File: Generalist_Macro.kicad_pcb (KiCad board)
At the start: 2 copper layers, 50.4 x 60.7 mm, 7 parts, among them SW1 SW_Push, SW2 SW_Push, SW3 SW_Push, SW4 SW_Push, U1 XIAO-RP2040-DIP

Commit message: Finished Schematic, Started PCB
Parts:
- removed SW4: SW_Push, Button_Switch_Keyboard:SW_Cherry_MX_1.00u_PCB
- added D10: WS2812B, LED_SMD:LED_WS2812B_PLCC4_5.0x5.0mm_P3.2mm, F.Cu at (160.0, 96.7)
- added D11: WS2812B, LED_SMD:LED_WS2812B_PLCC4_5.0x5.0mm_P3.2mm, F.Cu at (185.8, 63.2)
- added D12: WS2812B, LED_SMD:LED_WS2812B_PLCC4_5.0x5.0mm_P3.2mm, F.Cu at (185.8, 69.8)
- added D13: WS2812B, LED_SMD:LED_WS2812B_PLCC4_5.0x5.0mm_P3.2mm, F.Cu at (101.0, 56.0)
- added D14: WS2812B, LED_SMD:LED_WS2812B_PLCC4_5.0x5.0mm_P3.2mm, F.Cu at (160.2, 83.2)
- added D15: WS2812B, LED_SMD:LED_WS2812B_PLCC4_5.0x5.0mm_P3.2mm, F.Cu at (193.9, 63.2)
- added D16: WS2812B, LED_SMD:LED_WS2812B_PLCC4_5.0x5.0mm_P3.2mm, F.Cu at (193.9, 69.8)
- added D17: WS2812B, LED_SMD:LED_WS2812B_PLCC4_5.0x5.0mm_P3.2mm, F.Cu at (116.2, 56.0)
- added D18: WS2812B, LED_SMD:LED_WS2812B_PLCC4_5.0x5.0mm_P3.2mm, F.Cu at (160.2, 69.7)
- added D19: WS2812B, LED_SMD:LED_WS2812B_PLCC4_5.0x5.0mm_P3.2mm, F.Cu at (202.1, 63.2)
- added D20: WS2812B, LED_SMD:LED_WS2812B_PLCC4_5.0x5.0mm_P3.2mm, F.Cu at (202.1, 69.8)
- added D21: WS2812B, LED_SMD:LED_WS2812B_PLCC4_5.0x5.0mm_P3.2mm, F.Cu at (131.5, 56.0)
- added D22: WS2812B, LED_SMD:LED_WS2812B_PLCC4_5.0x5.0mm_P3.2mm, F.Cu at (160.6, 56.2)
- added D23: WS2812B, LED_SMD:LED_WS2812B_PLCC4_5.0x5.0mm_P3.2mm, F.Cu at (210.2, 63.2)
- added D24: WS2812B, LED_SMD:LED_WS2812B_PLCC4_5.0x5.0mm_P3.2mm, F.Cu at (210.2, 69.8)
- added D3: 1N4148WT, Diode_SMD:D_SOD-523, F.Cu at (64.5, 89.8)
- added D4: 1N4148WT, Diode_SMD:D_SOD-523, F.Cu at (74.0, 89.8)
- added D5: 1N4148WT, Diode_SMD:D_SOD-523, F.Cu at (64.5, 82.9)
- added D6: 1N4148WT, Diode_SMD:D_SOD-523, F.Cu at (74.0, 82.9)
- added D7: 1N4148WT, Diode_SMD:D_SOD-523, F.Cu at (74.0, 76.0)
- added D8: 1N4148WT, Diode_SMD:D_SOD-523, F.Cu at (64.5, 76.0)
- added D9: WS2812B, LED_SMD:LED_WS2812B_PLCC4_5.0x5.0mm_P3.2mm, F.Cu at (85.7, 56.0)
- added J1: OLED_DISPLAY, Connector_PinHeader_2.54mm:PinHeader_1x04_P2.54mm_Vertical, F.Cu at (141.4, 56.6)
- added SW13: RotaryEncoder_Switch, Rotary_Encoder:RotaryEncoder_Alps_EC11E-Switch_Vertical_H20mm, F.Cu at (137.8, 68.1)
- added SW5: SW_Push, Button_Switch_Keyboard:SW_Cherry_MX_1.00u_PCB, F.Cu at (141.8, 94.8)
- added SW6: SW_Push, Button_Switch_Keyboard:SW_Cherry_MX_1.00u_PCB, F.Cu at (88.9, 75.9)
- added SW7: SW_Push, Button_Switch_Keyboard:SW_Cherry_MX_1.00u_PCB, F.Cu at (104.0, 75.9)
- added SW8: SW_Push, Button_Switch_Keyboard:SW_Cherry_MX_1.00u_PCB, F.Cu at (122.9, 75.9)
- D1, D2: value SK6812MINI -> 1N4148WT; footprint LED_SMD:LED_SK6812MINI_PLCC4_3.5x3.5mm_P1.75mm -> Diode_SMD:D_SOD-523
- moved D2 155.5 mm to (64.5, 96.7), turned to 180 degrees
- moved U1 135.0 mm to (69.2, 61.7)
- moved D1 113.1 mm to (74.0, 96.7), turned to 180 degrees
- moved SW2 110.8 mm to (103.8, 95.0), turned to 180 degrees
- moved SW1 106.8 mm to (88.7, 95.0), turned to 180 degrees
- moved SW3 76.5 mm to (122.8, 94.9), turned to 180 degrees
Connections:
- D1 pad 1: Net-(D1-DOUT) -> Net-(D1-K)
- D1 pad 2: GND -> Net-(D1-A)
- D2 pad 1: unconnected-(D2-DOUT-Pad1) -> Net-(D1-K)
- D2 pad 2: GND -> Net-(D2-A)
- SW1 pad 1: GND -> Net-(D1-A)
- SW1 pad 2: Net-(U1-GPIO1/RX) -> Net-(U1-GPIO26/ADC0/A0)
- SW2 pad 1: GND -> Net-(D2-A)
- SW2 pad 2: Net-(U1-GPIO2/SCK) -> Net-(U1-GPIO27/ADC1/A1)
- SW3 pad 1: GND -> Net-(D3-A)
- SW3 pad 2: Net-(U1-GPIO4/MISO) -> Net-(U1-GPIO28/ADC2/A2)
- U1 pad 1: unconnected-(U1-GPIO26/ADC0/A0-Pad1) -> Net-(U1-GPIO26/ADC0/A0)
- U1 pad 10: Net-(U1-GPIO4/MISO) -> Net-(U1-GPIO3/MOSI)
- U1 pad 2: unconnected-(U1-GPIO27/ADC1/A1-Pad2) -> Net-(U1-GPIO27/ADC1/A1)
- U1 pad 3: unconnected-(U1-GPIO28/ADC2/A2-Pad3) -> Net-(U1-GPIO28/ADC2/A2)
- U1 pad 4: unconnected-(U1-GPIO29/ADC3/A3-Pad4) -> Net-(U1-GPIO29/ADC3/A3)
- U1 pad 5: Net-(D1-DIN) -> Net-(J1-Pin_1)
- U1 pad 6: unconnected-(U1-GPIO7/SCL-Pad6) -> Net-(J1-Pin_2)
- U1 pad 7: unconnected-(U1-GPIO0/TX-Pad7) -> Net-(D1-K)
- U1 pad 8: Net-(U1-GPIO1/RX) -> Net-(D18-DIN)
- U1 pad 9: Net-(U1-GPIO2/SCK) -> Net-(D5-K)
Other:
- board outline removed

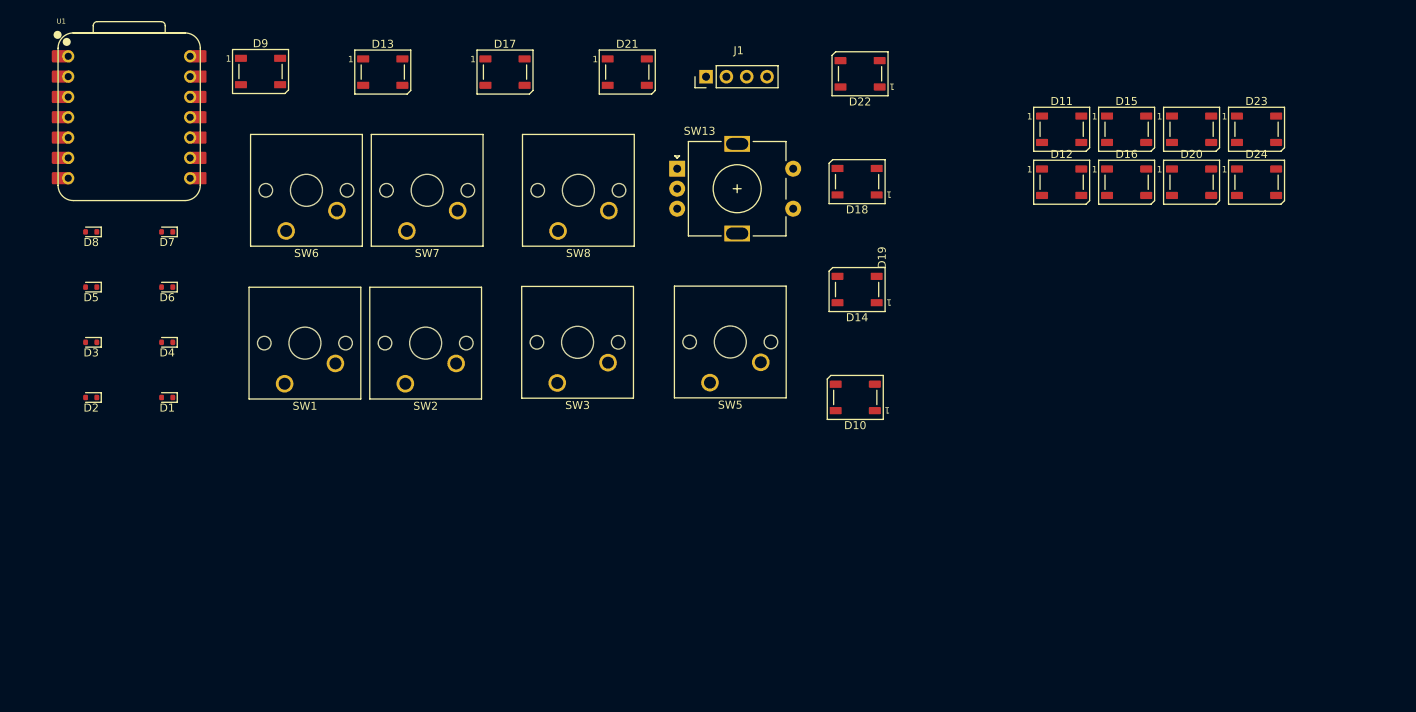
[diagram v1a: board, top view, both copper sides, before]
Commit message: PCB laid out and wired. I just have to add the **Aesthetic** silkscreens now
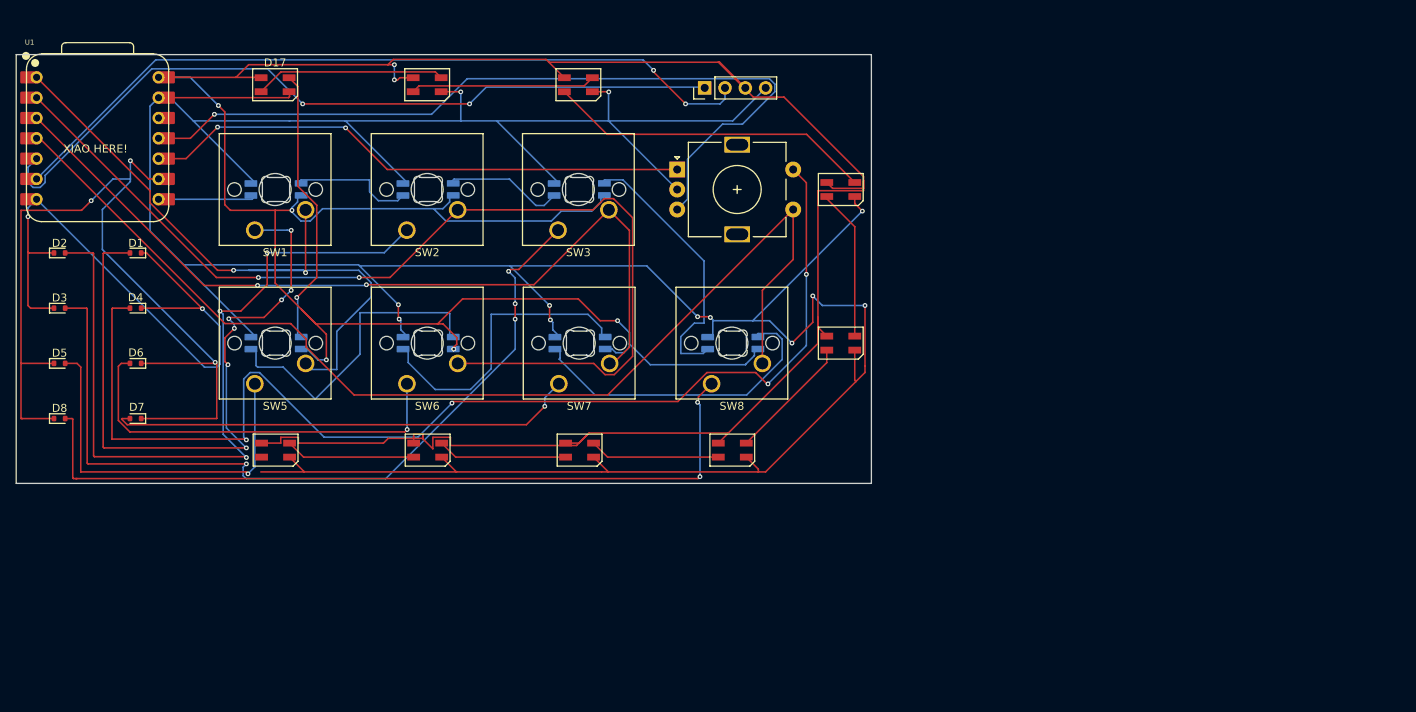
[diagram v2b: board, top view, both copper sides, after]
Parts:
- removed D9: WS2812B, LED_SMD:LED_WS2812B_PLCC4_5.0x5.0mm_P3.2mm
- added D25: WS2812B, LED_SMD:LED_SK6812MINI_PLCC4_3.5x3.5mm_P1.75mm, F.Cu at (87.5, 103.3)
- D10, D11, D12, D13, D14, D15, D16: footprint LED_SMD:LED_WS2812B_PLCC4_5.0x5.0mm_P3.2mm -> Backlight:MX_SK6812MINI-E_REV
- D17, D18, D19, D20, D21, D22, D23, D24: footprint LED_SMD:LED_WS2812B_PLCC4_5.0x5.0mm_P3.2mm -> LED_SMD:LED_SK6812MINI_PLCC4_3.5x3.5mm_P1.75mm
- moved D24 108.9 mm to (106.6, 103.3)
- moved D16 108.2 mm to (87.6, 89.9)
- moved D23 93.6 mm to (125.5, 103.3)
- moved D15 91.3 mm to (106.6, 89.9)
- moved D11 79.6 mm to (106.6, 70.7)
- moved D10 76.9 mm to (87.6, 70.7), turned to 0 degrees
- moved D19 76.9 mm to (125.4, 57.6)
- moved D12 60.3 mm to (125.5, 70.7)
- moved SW5 56.9 mm to (85.0, 95.0)
- moved D13 55.3 mm to (144.7, 89.9)
- moved D18 55.1 mm to (106.5, 57.6), turned to 0 degrees
- moved D22 49.7 mm to (144.6, 103.3), turned to 0 degrees
- moved D20 43.9 mm to (158.2, 70.7)
- moved D21 43.1 mm to (158.2, 89.9)
- moved D14 35.3 mm to (125.6, 89.9), turned to 0 degrees
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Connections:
- net Net-(D1-K) renamed Row 1
- net Net-(D5-K) renamed Row 2
- net Net-(J1-Pin_1) renamed SDA
- net Net-(J1-Pin_2) renamed SCL
- net Net-(U1-GPIO26/ADC0/A0) renamed Column 1
- net Net-(U1-GPIO27/ADC1/A1) renamed Column 2
- net Net-(U1-GPIO28/ADC2/A2) renamed Column 3
- net Net-(U1-GPIO29/ADC3/A3) renamed Column 4
- D16 pad 4: Net-(D16-DIN) -> Net-(D15-DOUT)
- D17 pad 2: unconnected-(D17-DOUT-Pad2) -> Net-(D17-DOUT)
- D17 pad 4: Net-(D15-DOUT) -> Net-(D16-DOUT)
- D18 pad 4: Net-(D18-DIN) -> Net-(D17-DOUT)
- D20 pad 4: Net-(D20-DIN) -> Net-(D19-DOUT)
- D21 pad 2: Net-(D20-DIN) -> Net-(D21-DOUT)
- D21 pad 4: Net-(D21-DIN) -> Net-(D20-DOUT)
- D22 pad 2: Net-(D16-DIN) -> Net-(D22-DOUT)
- D22 pad 4: Net-(D19-DOUT) -> Net-(D21-DOUT)
- D23 pad 2: Net-(D21-DIN) -> Net-(D23-DOUT)
- D23 pad 4: Net-(D23-DIN) -> Net-(D22-DOUT)
- D24 pad 1: unconnected-(D24-VDD-Pad1) -> +5V
- D24 pad 2: Net-(D23-DIN) -> Net-(D24-DOUT)
- D24 pad 4: Net-(D16-DOUT) -> Net-(D23-DOUT)
- SW13 pad A: Net-(U1-GPIO3/MOSI) -> Rotary A
- SW13 pad B: Net-(U1-GPIO3/MOSI) -> Rotary B
- U1 pad 10: Net-(U1-GPIO3/MOSI) -> Rotary A
- U1 pad 11: Net-(U1-GPIO3/MOSI) -> Rotary B
- U1 pad 8: Net-(D18-DIN) -> Net-(D10-DIN)
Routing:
- net GND: track 0.00 -> 432.1 mm, vias 0 -> 12
- net +5V: track 0.00 -> 410.6 mm, vias 0 -> 7
- net Net-(D4-A): track 0.00 -> 145.8 mm, vias 0 -> 4
- net Column 4: track 0.00 -> 139.7 mm
- net Column 2: track 0.00 -> 129.6 mm, vias 0 -> 2
- net Row 2: track 0.00 -> 113.2 mm, vias 0 -> 3
- net Column 3: track 0.00 -> 105.7 mm, vias 0 -> 2
- net Net-(D3-A): track 0.00 -> 102.9 mm, vias 0 -> 4
- net Rotary B: track 0.00 -> 101.8 mm, vias 0 -> 1
- net Net-(D8-A): track 0.00 -> 99.5 mm, vias 0 -> 2
- net Net-(D2-A): track 0.00 -> 97.8 mm, vias 0 -> 3
- net SDA: track 0.00 -> 97.6 mm, vias 0 -> 2
- net SCL: track 0.00 -> 96.2 mm, vias 0 -> 2
- net Column 1: track 0.00 -> 85.3 mm, vias 0 -> 2
- net Net-(D1-A): track 0.00 -> 85.0 mm, vias 0 -> 7
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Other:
- board outline added: 106.9 x 53.6 mm
- board text added: "D1"
- board text added: "D7"
- board text added: "XIAO HERE!"
